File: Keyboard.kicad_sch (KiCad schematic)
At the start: 32 parts, among them J1 Conn_01x05_Male, K6 SW_SPST, P7 1M, Q15 Q_PNP_BCE, Q16 BF244A, Q17 BF244A, Q18 BF244A, Q19 BF244A, U3 uA741-DIP14

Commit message: Fix PCB errors
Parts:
- added A_Sin1, B_Sin1, C_Sin1, D_Sin1, GATE1, P7-1-3, P7-2: Conn_01x01, Connector_PinHeader_2.54mm:PinHeader_1x01_P2.54mm_Vertical, symbol Connector_Generic:Conn_01x01
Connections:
- net -VSW: now also R85.2
- net A: now also A_Sin1.1 (Pin_1)
- net B: now also B_Sin1.1 (Pin_1)
- net C: now also C_Sin1.1 (Pin_1)
- net D: now also D_Sin1.1 (Pin_1)
- net GATE: now also GATE1.1 (Pin_1)
- net GND: no longer R85.2
- net at P7.1, P7.2, R88.1: now also P7-1-3.1 (Pin_1)
- net at P7.3, Q19.2 (G): now also P7-2.1 (Pin_1)
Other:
- moved on the sheet: R77

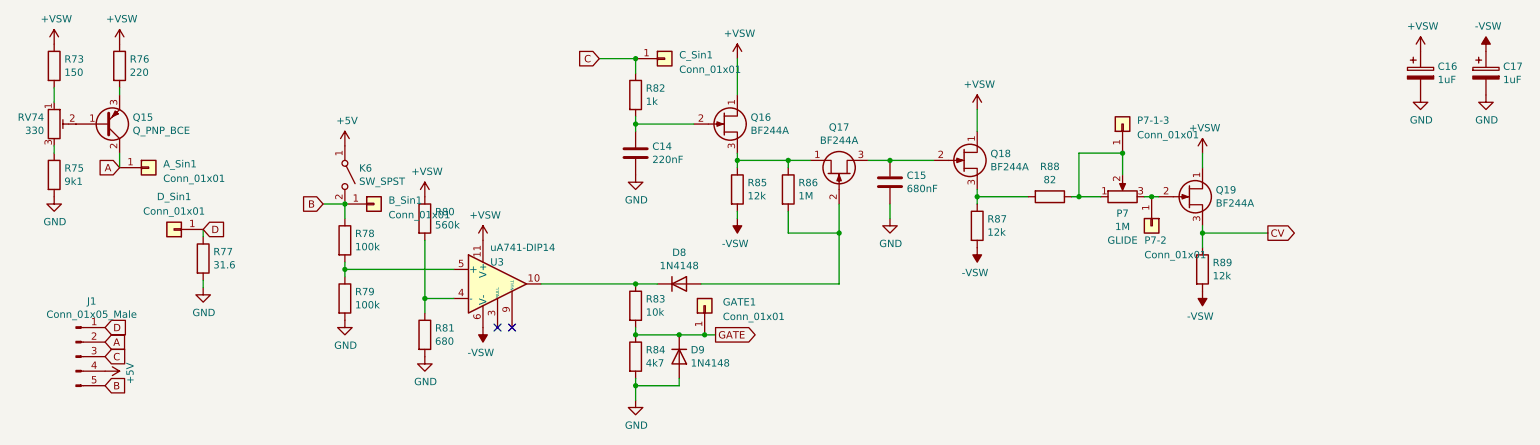
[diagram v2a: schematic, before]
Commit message: Replace symbols with new library
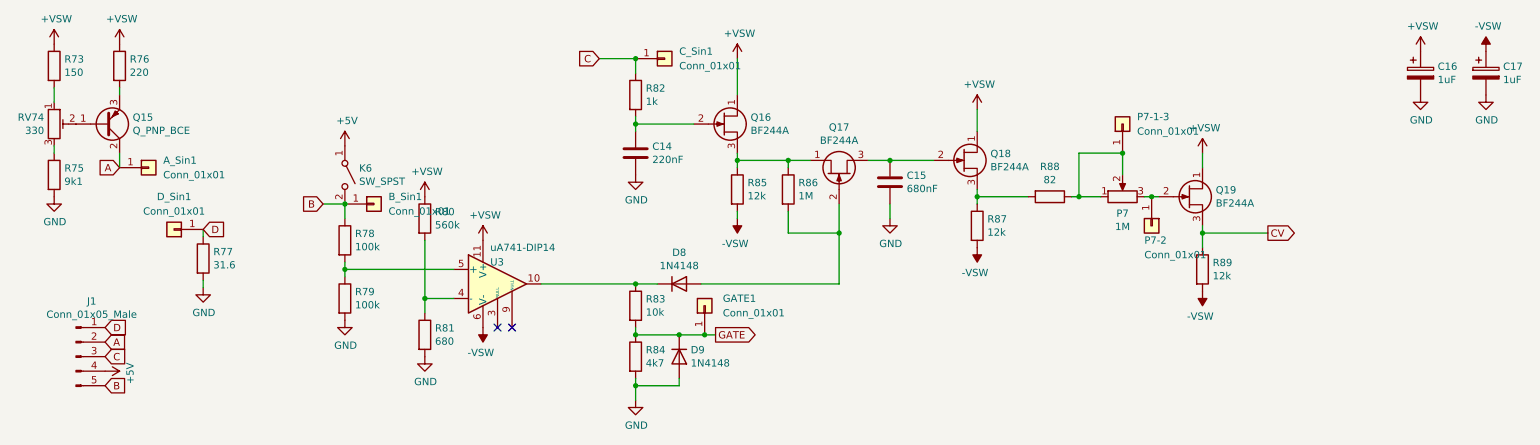
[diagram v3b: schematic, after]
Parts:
- A_Sin1, B_Sin1, C_Sin1, D_Sin1, GATE1, P7-1-3, P7-2: footprint Connector_PinHeader_2.54mm:PinHeader_1x01_P2.54mm_Vertical -> (none)
- C14, C15: footprint Capacitor_THT:C_Disc_D5.0mm_W2.5mm_P5.00mm -> (none)
- C16, C17: footprint Capacitor_THT:CP_Radial_D6.3mm_P2.50mm -> (none)
- D8, D9: footprint Diode_THT:D_A-405_P10.16mm_Horizontal -> (none)
- J1: footprint Connector_PinHeader_2.54mm:PinHeader_1x05_P2.54mm_Vertical -> (none)
- K6: footprint Connector_PinSocket_2.54mm:PinSocket_1x03_P2.54mm_Vertical -> (none)
- P7: footprint Connector_PinSocket_2.54mm:PinSocket_1x03_P2.54mm_Vertical -> (none); Label GLIDE -> (none)
- Q15: symbol Device:Q_PNP_BCE -> Transistor_BJT:Q_PNP_BCE
- Q16, Q19: footprint Package_TO_SOT_THT:TO-92L_Inline_Wide -> Package_TO_SOT_THT:TO-92_Inline
- Q17, Q18: footprint Package_TO_SOT_THT:TO-218-3_Vertical -> Package_TO_SOT_THT:TO-92_Inline
- R73, R75, R76, R77, R78, R79, R80, R81, R82, R83, R84, R85, R86, R87, R88, R89: footprint Resistor_THT:R_Axial_DIN0207_L6.3mm_D2.5mm_P15.24mm_Horizontal -> (none)
- RV74: footprint Potentiometer_THT:Potentiometer_Bourns_3296W_Vertical -> (none)
- U3: footprint Package_DIP:DIP-14_W7.62mm_Socket_LongPads -> (none)

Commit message: Label connectors, update footprints
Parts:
- A_Sin1, B_Sin1, C_Sin1, D_Sin1, GATE1, P7-1-3, P7-2: footprint (none) -> Connector_PinHeader_2.54mm:PinHeader_1x01_P2.54mm_Vertical
- C14, C15: footprint (none) -> Capacitor_THT:C_Disc_D5.0mm_W2.5mm_P5.00mm
- C16, C17: footprint (none) -> Capacitor_THT:CP_Radial_D6.3mm_P2.50mm
- D8, D9: footprint (none) -> Diode_THT:D_A-405_P10.16mm_Horizontal
- Q16, Q19: footprint Package_TO_SOT_THT:TO-92_Inline -> Package_TO_SOT_THT:TO-92_Inline_Wide
- Q17: footprint Package_TO_SOT_THT:TO-92_Inline -> PCM_Package_TO_SOT_THT_AKL:TO-92_Inline_Wide_SGD
- R73, R75, R76, R77, R78, R79, R80, R81, R82, R83, R84, R85, R86, R87, R88, R89: footprint (none) -> Resistor_THT:R_Axial_DIN0207_L6.3mm_D2.5mm_P15.24mm_Horizontal
- RV74: footprint (none) -> Potentiometer_THT:Potentiometer_Bourns_3296W_Vertical
- U3: footprint (none) -> Package_DIP:DIP-14_W7.62mm_Socket_LongPads
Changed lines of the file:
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@@
 			)
 		)
-		(property "Footprint" ""
+		(property "Footprint" "Resistor_THT:R_Axial_DIN0207_L6.3mm_D2.5mm_P15.24mm_Horizontal"
 			(at 18.542 27.94 90)
 			(effects
@@
 			)
 		)
-		(property "Footprint" ""
+		(property "Footprint" "Resistor_THT:R_Axial_DIN0207_L6.3mm_D2.5mm_P15.24mm_Horizontal"
 			(at 18.542 46.99 90)
 			(effects
@@
 			)
 		)
-		(property "Footprint" ""
+		(property "Footprint" "Potentiometer_THT:Potentiometer_Bourns_3296W_Vertical"
 			(at 20.32 38.1 0)
 			(effects
@@
 			)
 		)
-		(property "Footprint" ""
+		(property "Footprint" "Resistor_THT:R_Axial_DIN0207_L6.3mm_D2.5mm_P15.24mm_Horizontal"
 			(at 29.972 27.94 90)
 			(effects
@@
 			)
 		)
-		(property "Footprint" ""
+		(property "Footprint" "Capacitor_THT:CP_Radial_D6.3mm_P2.50mm"
 			(at 260.0452 33.02 0)
 			(effects
@@
 			)
 		)
-		(property "Footprint" ""
+		(property "Footprint" "Resistor_THT:R_Axial_DIN0207_L6.3mm_D2.5mm_P15.24mm_Horizontal"
 			(at 69.342 58.42 90)
 			(effects
@@
 			)
 		)
-		(property "Footprint" ""
+		(property "Footprint" "Resistor_THT:R_Axial_DIN0207_L6.3mm_D2.5mm_P15.24mm_Horizontal"
 			(at 69.342 68.58 90)
 			(effects
@@
 			)
 		)
-		(property "Footprint" ""
+		(property "Footprint" "Package_DIP:DIP-14_W7.62mm_Socket_LongPads"
 			(at 99.06 64.77 0)
 			(effects
@@
 			)
 		)
-		(property "Footprint" ""
+		(property "Footprint" "Resistor_THT:R_Axial_DIN0207_L6.3mm_D2.5mm_P15.24mm_Horizontal"
 			(at 83.312 54.61 90)
 			(effects
@@
 			)
 		)
-		(property "Footprint" ""
+		(property "Footprint" "Resistor_THT:R_Axial_DIN0207_L6.3mm_D2.5mm_P15.24mm_Horizontal"
 			(at 83.312 74.93 90)
 			(effects
@@
 			)
 		)
-		(property "Footprint" ""
+		(property "Footprint" "Resistor_THT:R_Axial_DIN0207_L6.3mm_D2.5mm_P15.24mm_Horizontal"
 			(at 120.142 69.85 90)
 			(effects
@@
 			)
 		)
-		(property "Footprint" ""
+		(property "Footprint" "Resistor_THT:R_Axial_DIN0207_L6.3mm_D2.5mm_P15.24mm_Horizontal"
 			(at 120.142 78.74 90)
 			(effects
@@
 			)
 		)
-		(property "Footprint" ""
+		(property "Footprint" "Diode_THT:D_A-405_P10.16mm_Horizontal"
 			(at 129.54 78.74 0)
 			(effects
@@
 			)
 		)
-		(property "Footprint" ""
+		(property "Footprint" "Diode_THT:D_A-405_P10.16mm_Horizontal"
 			(at 129.54 66.04 0)
 			(effects
@@
 			)
 		)
-		(property "Footprint" "Package_TO_SOT_THT:TO-92_Inline"
+		(property "Footprint" "Package_TO_SOT_THT:TO-92_Inline_Wide"
 			(at 142.24 40.005 0)
 			(effects
@@
 			)
 		)
-		(property "Footprint" ""
+		(property "Footprint" "Resistor_THT:R_Axial_DIN0207_L6.3mm_D2.5mm_P15.24mm_Horizontal"
 			(at 120.142 33.02 90)
 			(effects
@@
 			)
 		)
-		(property "Footprint" ""
+		(property "Footprint" "Capacitor_THT:C_Disc_D5.0mm_W2.5mm_P5.00mm"
 			(at 122.8852 46.99 0)
 			(effects
@@
 			)
 		)
-		(property "Footprint" "Package_TO_SOT_THT:TO-92_Inline"
+		(property "Footprint" "PCM_Package_TO_SOT_THT_AKL:TO-92_Inline_Wide_SGD"
 			(at 159.385 41.91 0)
 			(effects
@@
 			)
 		)
-		(property "Footprint" ""
+		(property "Footprint" "Resistor_THT:R_Axial_DIN0207_L6.3mm_D2.5mm_P15.24mm_Horizontal"
 			(at 137.922 49.53 90)
 			(effects
@@
 			)
 		)
-		(property "Footprint" ""
+		(property "Footprint" "Resistor_THT:R_Axial_DIN0207_L6.3mm_D2.5mm_P15.24mm_Horizontal"
 			(at 146.812 49.53 90)
 			(effects
@@
 			)
 		)
-		(property "Footprint" ""
+		(property "Footprint" "Capacitor_THT:C_Disc_D5.0mm_W2.5mm_P5.00mm"
 			(at 167.3352 52.07 0)
 			(effects
@@
 			)
 		)
-		(property "Footprint" ""
+		(property "Footprint" "Capacitor_THT:CP_Radial_D6.3mm_P2.50mm"
 			(at 271.4752 33.02 0)
 			(effects
@@
 			)
 		)
-		(property "Footprint" ""
+		(property "Footprint" "Resistor_THT:R_Axial_DIN0207_L6.3mm_D2.5mm_P15.24mm_Horizontal"
 			(at 179.832 55.88 90)
 			(effects
@@
 			)
 		)
-		(property "Footprint" ""
+		(property "Footprint" "Resistor_THT:R_Axial_DIN0207_L6.3mm_D2.5mm_P15.24mm_Horizontal"
 			(at 194.31 49.022 90)
 			(effects
@@
 		(exclude_from_sim no)
 		(in_bom yes)
-		(on_board yes)
+		(on_board no)
 		(dnp no)
 		(property "Reference" "P7"
@@
 			)
 		)
-		(property "Footprint" "Package_TO_SOT_THT:TO-92_Inline"
+		(property "Footprint" "Package_TO_SOT_THT:TO-92_Inline_Wide"
 			(at 223.52 52.705 0)
 			(effects
@@
 			)
 		)
-		(property "Footprint" ""
+		(property "Footprint" "Resistor_THT:R_Axial_DIN0207_L6.3mm_D2.5mm_P15.24mm_Horizontal"
 			(at 219.202 63.5 90)
 			(effects
@@
 			)
 		)
-		(property "Footprint" ""
+		(property "Footprint" "Resistor_THT:R_Axial_DIN0207_L6.3mm_D2.5mm_P15.24mm_Horizontal"
 			(at 44.577 61.595 90)
 			(effects
@@
 			)
 		)
-		(property "Footprint" ""
+		(property "Footprint" "Connector_PinHeader_2.54mm:PinHeader_1x01_P2.54mm_Vertical"
 			(at 212.09 55.88 0)
 			(effects
@@
 			)
 		)
-		(property "Footprint" ""
+		(property "Footprint" "Connector_PinHeader_2.54mm:PinHeader_1x01_P2.54mm_Vertical"
 			(at 36.83 45.72 0)
 			(effects
@@
 			)
 		)
-		(property "Footprint" ""
+		(property "Footprint" "Connector_PinHeader_2.54mm:PinHeader_1x01_P2.54mm_Vertical"
 			(at 127 26.67 0)
 			(effects
@@
 			)
 		)
-		(property "Footprint" ""
+		(property "Footprint" "Connector_PinHeader_2.54mm:PinHeader_1x01_P2.54mm_Vertical"
 			(at 133.985 69.85 0)
 			(effects
@@
 			)
 		)
-		(property "Footprint" ""
+		(property "Footprint" "Connector_PinHeader_2.54mm:PinHeader_1x01_P2.54mm_Vertical"
 			(at 41.275 56.515 0)
 			(effects
@@
 			)
 		)
-		(property "Footprint" ""
+		(property "Footprint" "Connector_PinHeader_2.54mm:PinHeader_1x01_P2.54mm_Vertical"
 			(at 76.2 52.07 0)
 			(effects
@@
 			)
 		)
-		(property "Footprint" ""
+		(property "Footprint" "Connector_PinHeader_2.54mm:PinHeader_1x01_P2.54mm_Vertical"
 			(at 207.01 38.1 0)
 			(effects
